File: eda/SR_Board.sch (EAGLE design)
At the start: 14 parts

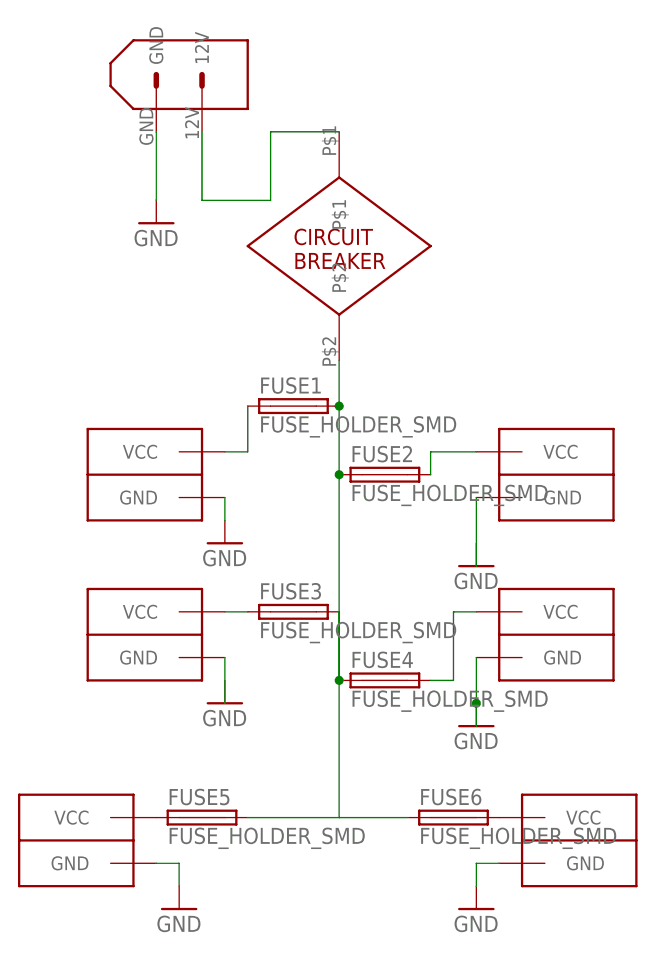
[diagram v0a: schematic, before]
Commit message: Moved Frame to origin. Replaced GND with GND from Pi library.
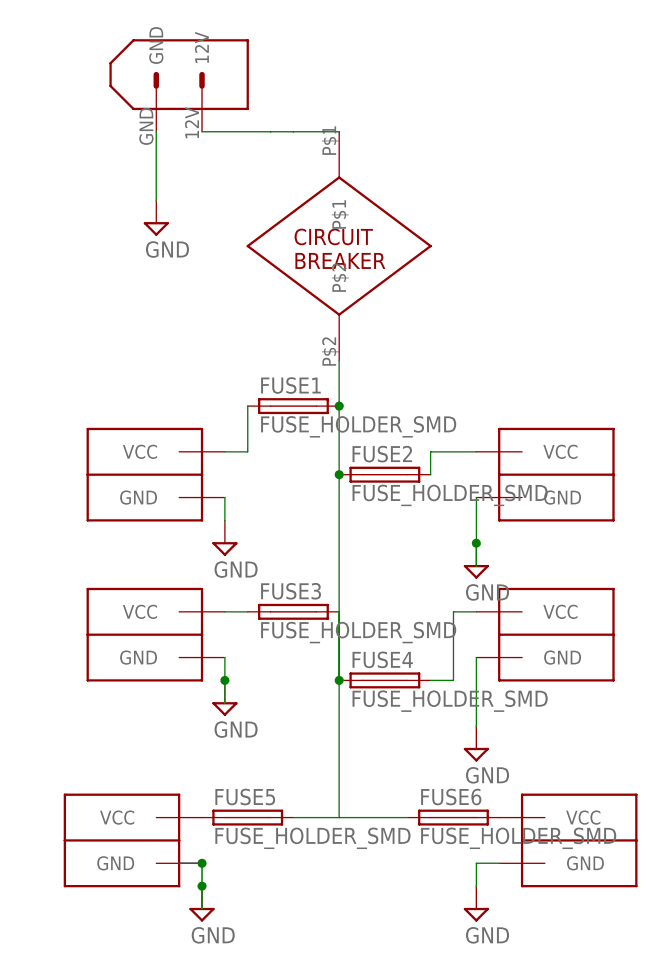
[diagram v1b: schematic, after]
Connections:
- removed net N$6: CONN4.GND
- removed net N$8: CONN1.GND
- net GND: now also CONN1.GND, CONN4.GND
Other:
- moved on the sheet: FUSE5
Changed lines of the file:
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@@
 <part name="CONN4" library="pie" deviceset="ANDERSON" device="HORIZONTAL"/>
 <part name="CONN5" library="pie" deviceset="ANDERSON" device="HORIZONTAL"/>
-<part name="GND1" library="SparkFun-Aesthetics" deviceset="GND" device=""/>
-<part name="GND2" library="SparkFun-Aesthetics" deviceset="GND" device=""/>
-<part name="GND3" library="SparkFun-Aesthetics" deviceset="GND" device=""/>
-<part name="GND4" library="SparkFun-Aesthetics" deviceset="GND" device=""/>
-<part name="GND5" library="SparkFun-Aesthetics" deviceset="GND" device=""/>
 <part name="CIRCUIT_BREAKER" library="pie" deviceset="CIRC_BREAKER" device=""/>
 <part name="FUSE2" library="pie" deviceset="FUSE_HOLDER_SMD" device=""/>
@@
 <part name="CONN3" library="pie" deviceset="ANDERSON" device="HORIZONTAL"/>
 <part name="CONN6" library="pie" deviceset="ANDERSON" device="HORIZONTAL"/>
-<part name="GND6" library="SparkFun-Aesthetics" deviceset="GND" device=""/>
-<part name="GND7" library="SparkFun-Aesthetics" deviceset="GND" device=""/>
+<part name="SUPPLY1" library="pie" deviceset="GND" device=""/>
+<part name="SUPPLY2" library="pie" deviceset="GND" device=""/>
+<part name="SUPPLY3" library="pie" deviceset="GND" device=""/>
+<part name="SUPPLY4" library="pie" deviceset="GND" device=""/>
+<part name="SUPPLY5" library="pie" deviceset="GND" device=""/>
+<part name="SUPPLY6" library="pie" deviceset="GND" device=""/>
+<part name="SUPPLY7" library="pie" deviceset="GND" device=""/>
 </parts>
 <sheets>
@@
 </plain>
 <instances>
-<instance part="FRAME1" gate="G$1" x="-15.24" y="-38.1"/>
-<instance part="FRAME1" gate="G$2" x="132.08" y="-38.1"/>
+<instance part="FRAME1" gate="G$1" x="0" y="0"/>
+<instance part="FRAME1" gate="G$2" x="147.32" y="0"/>
 <instance part="U$1" gate="G$1" x="12.7" y="111.76" rot="R180"/>
 <instance part="CONN1" gate="G$1" x="10.16" y="48.26"/>
@@
 <instance part="CONN4" gate="G$1" x="53.34" y="66.04" rot="MR0"/>
 <instance part="CONN5" gate="G$1" x="53.34" y="48.26" rot="MR0"/>
-<instance part="GND1" gate="1" x="10.16" y="93.98"/>
-<instance part="GND2" gate="1" x="17.78" y="58.42"/>
-<instance part="GND3" gate="1" x="17.78" y="40.64"/>
-<instance part="GND4" gate="1" x="45.72" y="38.1"/>
-<instance part="GND5" gate="1" x="45.72" y="55.88"/>
 <instance part="CIRCUIT_BREAKER" gate="G$1" x="30.48" y="91.44"/>
 <instance part="FUSE2" gate="G$1" x="35.56" y="66.04"/>
@@
 <instance part="FUSE3" gate="G$1" x="25.4" y="50.8"/>
 <instance part="FUSE4" gate="G$1" x="35.56" y="43.18"/>
-<instance part="FUSE5" gate="G$1" x="15.24" y="27.94"/>
+<instance part="FUSE5" gate="G$1" x="20.32" y="27.94"/>
 <instance part="FUSE6" gate="G$1" x="43.18" y="27.94"/>
-<instance part="CONN3" gate="G$1" x="2.54" y="25.4"/>
+<instance part="CONN3" gate="G$1" x="7.62" y="25.4"/>
 <instance part="CONN6" gate="G$1" x="55.88" y="25.4" rot="MR0"/>
-<instance part="GND6" gate="1" x="12.7" y="17.78"/>
-<instance part="GND7" gate="1" x="45.72" y="17.78"/>
+<instance part="SUPPLY1" gate="GND" x="17.78" y="58.42"/>
+<instance part="SUPPLY2" gate="GND" x="45.72" y="55.88"/>
+<instance part="SUPPLY3" gate="GND" x="10.16" y="93.98"/>
+<instance part="SUPPLY4" gate="GND" x="17.78" y="40.64"/>
+<instance part="SUPPLY5" gate="GND" x="45.72" y="35.56"/>
+<instance part="SUPPLY6" gate="GND" x="15.24" y="17.78"/>
+<instance part="SUPPLY7" gate="GND" x="45.72" y="17.78"/>
 </instances>
 <busses>
 </busses>
 <nets>
-<net name="GND" class="0">
-<segment>
-<pinref part="U$1" gate="G$1" pin="GND"/>
-<pinref part="GND1" gate="1" pin="GND"/>
-<wire x1="10.16" y1="104.14" x2="10.16" y2="96.52" width="0.1524" layer="91"/>
-</segment>
-<segment>
-<pinref part="GND2" gate="1" pin="GND"/>
-<pinref part="CONN2" gate="G$1" pin="GND"/>
-<wire x1="17.78" y1="60.96" x2="17.78" y2="63.5" width="0.1524" layer="91"/>
-</segment>
-<segment>
-<pinref part="CONN5" gate="G$1" pin="GND"/>
-<wire x1="45.72" y1="45.72" x2="45.72" y2="40.64" width="0.1524" layer="91"/>
-<pinref part="GND4" gate="1" pin="GND"/>
-<wire x1="45.72" y1="40.64" x2="45.72" y2="38.1" width="0.1524" layer="91"/>
-<junction x="45.72" y="40.64"/>
-</segment>
-<segment>
-<pinref part="CONN3" gate="G$1" pin="GND"/>
-<wire x1="10.16" y1="22.86" x2="12.7" y2="22.86" width="0.1524" layer="91"/>
-<pinref part="GND6" gate="1" pin="GND"/>
-<wire x1="12.7" y1="22.86" x2="12.7" y2="20.32" width="0.1524" layer="91"/>
-</segment>
-<segment>
-<pinref part="CONN6" gate="G$1" pin="GND"/>
-<wire x1="48.26" y1="22.86" x2="45.72" y2="22.86" width="0.1524" layer="91"/>
-<pinref part="GND7" gate="1" pin="GND"/>
-<wire x1="45.72" y1="22.86" x2="45.72" y2="20.32" width="0.1524" layer="91"/>
-</segment>
-</net>
 <net name="12V" class="0">
 <segment>
@@
 <wire x1="30.48" y1="43.18" x2="30.48" y2="27.94" width="0.1524" layer="91"/>
 <wire x1="30.48" y1="27.94" x2="38.1" y2="27.94" width="0.1524" layer="91"/>
-<wire x1="30.48" y1="27.94" x2="20.32" y2="27.94" width="0.1524" layer="91"/>
+<wire x1="30.48" y1="27.94" x2="25.4" y2="27.94" width="0.1524" layer="91"/>
 <pinref part="FUSE5" gate="G$1" pin="2"/>
 <pinref part="FUSE6" gate="G$1" pin="1"/>
@@
 </segment>
 </net>
-<net name="N$8" class="0">
-<segment>
-<pinref part="CONN1" gate="G$1" pin="GND"/>
-<wire x1="17.78" y1="40.64" x2="17.78" y2="45.72" width="0.1524" layer="91"/>
-</segment>
-</net>
 <net name="N$5" class="0">
 <segment>
@@
 <pinref part="FUSE2" gate="G$1" pin="2"/>
 <wire x1="40.64" y1="68.58" x2="40.64" y2="66.04" width="0.1524" layer="91"/>
-</segment>
-</net>
-<net name="N$6" class="0">
-<segment>
-<pinref part="CONN4" gate="G$1" pin="GND"/>
-<wire x1="45.72" y1="63.5" x2="45.72" y2="55.88" width="0.1524" layer="91"/>
 </segment>
 </net>
@@
 <net name="BAT" class="0">
 <segment>
+<pinref part="CIRCUIT_BREAKER" gate="G$1" pin="P$1"/>
+<wire x1="22.86" y1="104.14" x2="25.4" y2="104.14" width="0.1524" layer="91"/>
 <pinref part="U$1" gate="G$1" pin="12V"/>
-<wire x1="15.24" y1="104.14" x2="15.24" y2="96.52" width="0.1524" layer="91"/>
-<wire x1="15.24" y1="96.52" x2="22.86" y2="96.52" width="0.1524" layer="91"/>
-<wire x1="22.86" y1="96.52" x2="22.86" y2="104.14" width="0.1524" layer="91"/>
-<pinref part="CIRCUIT_BREAKER" gate="G$1" pin="P$1"/>
-<wire x1="22.86" y1="104.14" x2="30.48" y2="104.14" width="0.1524" layer="91"/>
+<wire x1="25.4" y1="104.14" x2="30.48" y2="104.14" width="0.1524" layer="91"/>
+<wire x1="15.24" y1="104.14" x2="22.86" y2="104.14" width="0.1524" layer="91"/>
 </segment>
 </net>
+<net name="GND" class="0">
+<segment>
+<pinref part="U$1" gate="G$1" pin="GND"/>
+<wire x1="10.16" y1="104.14" x2="10.16" y2="96.52" width="0.1524" layer="91"/>
+<pinref part="SUPPLY3" gate="GND" pin="GND"/>
+</segment>
+<segment>
+<pinref part="CONN2" gate="G$1" pin="GND"/>
+<wire x1="17.78" y1="60.96" x2="17.78" y2="63.5" width="0.1524" layer="91"/>
+<pinref part="SUPPLY1" gate="GND" pin="GND"/>
+</segment>
+<segment>
+<pinref part="CONN4" gate="G$1" pin="GND"/>
+<wire x1="45.72" y1="63.5" x2="45.72" y2="58.42" width="0.1524" layer="91"/>
+<pinref part="SUPPLY2" gate="GND" pin="GND"/>
+<wire x1="45.72" y1="58.42" x2="45.72" y2="55.88" width="0.1524" layer="91"/>
+<junction x="45.72" y="58.42"/>
+</segment>
+<segment>
+<pinref part="CONN1" gate="G$1" pin="GND"/>
+<wire x1="17.78" y1="40.64" x2="17.78" y2="43.18" width="0.1524" layer="91"/>
+<pinref part="SUPPLY4" gate="GND" pin="GND"/>
+<wire x1="17.78" y1="43.18" x2="17.78" y2="45.72" width="0.1524" layer="91"/>
+<junction x="17.78" y="43.18"/>
+</segment>
+<segment>
+<pinref part="CONN5" gate="G$1" pin="GND"/>
+<wire x1="45.72" y1="45.72" x2="45.72" y2="38.1" width="0.1524" layer="91"/>
+<pinref part="SUPPLY5" gate="GND" pin="GND"/>
+</segment>
+<segment>
+<pinref part="CONN3" gate="G$1" pin="GND"/>
+<wire x1="15.24" y1="22.86" x2="12.7" y2="22.86" width="0.1524" layer="91"/>
+<wire x1="15.24" y1="22.86" x2="15.24" y2="20.32" width="0.1524" layer="91"/>
+<junction x="15.24" y="22.86"/>
+<pinref part="SUPPLY6" gate="GND" pin="GND"/>
+<wire x1="15.24" y1="20.32" x2="15.24" y2="17.78" width="0.1524" layer="91"/>
+<junction x="15.24" y="20.32"/>
+</segment>
+<segment>
+<pinref part="CONN6" gate="G$1" pin="GND"/>
+<wire x1="48.26" y1="22.86" x2="45.72" y2="22.86" width="0.1524" layer="91"/>
+<wire x1="45.72" y1="22.86" x2="45.72" y2="20.32" width="0.1524" layer="91"/>
+<pinref part="SUPPLY7" gate="GND" pin="GND"/>
+</segment>
+</net>
